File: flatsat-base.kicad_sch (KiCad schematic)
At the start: 13 parts, among them J1 xf2m-2415-1a-symbols, J10 Conn_01x24_Male, J11 Conn_02x05_Odd_Even, J12 Conn_02x05_Odd_Even, J13 Conn_01x10_Male, J2 XF2M-1015-1A-symbols, J3 XF2M-1015-1A-symbols, J4 XF2M-1015-1A-symbols, J5 XF2M-1015-1A-symbols, J6 XF2M-1015-1A-symbols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

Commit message: PCB outline and footprint locations defined, needs routing
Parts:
- J1: footprint PyCubed Main:XF2M-2415-1A -> PyCubed-Mini Main:XF2M-2415-1A
- J13: footprint Connector_PinHeader_1.27mm:PinHeader_1x10_P1.27mm_Vertical -> Connector_PinHeader_2.54mm:PinHeader_1x10_P2.54mm_Vertical
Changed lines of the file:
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@@
       (effects (font (size 1.27 1.27)) (justify right))
     )
-    (property "Footprint" "Connector_PinHeader_1.27mm:PinHeader_1x10_P1.27mm_Vertical" (id 2) (at 101.6 177.8 0)
+    (property "Footprint" "Connector_PinHeader_2.54mm:PinHeader_1x10_P2.54mm_Vertical" (id 2) (at 101.6 177.8 0)
       (effects (font (size 1.27 1.27)) hide)
     )
@@
     (property "Reference" "J1" (id 0) (at 54.61 30.48 0))
     (property "Value" "xf2m-2415-1a-symbols" (id 1) (at 54.61 33.02 0))
-    (property "Footprint" "PyCubed Main:XF2M-2415-1A" (id 2) (at 62.23 35.56 0)
+    (property "Footprint" "PyCubed-Mini Main:XF2M-2415-1A" (id 2) (at 62.23 35.56 0)
       (effects (font (size 1.27 1.27)) (justify left) hide)
     )
@@
     )
     (path "/eefa62b0-7985-4153-9454-98c24aeb544a"
-      (reference "J1") (unit 1) (value "xf2m-2415-1a-symbols") (footprint "PyCubed Main:XF2M-2415-1A")
+      (reference "J1") (unit 1) (value "xf2m-2415-1a-symbols") (footprint "PyCubed-Mini Main:XF2M-2415-1A")
     )
     (path "/405f63ce-92fd-4885-8744-aea1af979a53"
@@
     )
     (path "/cabb4d71-b835-4085-a569-a6974d8b4662"
-      (reference "J13") (unit 1) (value "Conn_01x10_Male") (footprint "Connector_PinHeader_1.27mm:PinHeader_1x10_P1.27mm_Vertical")
-    )
-  )
+      (reference "J13") (unit 1) (value "Conn_01x10_Male") (footprint "Connector_PinHeader_2.54mm:PinHeader_1x10_P2.54mm_Vertical")
+    )
+  )

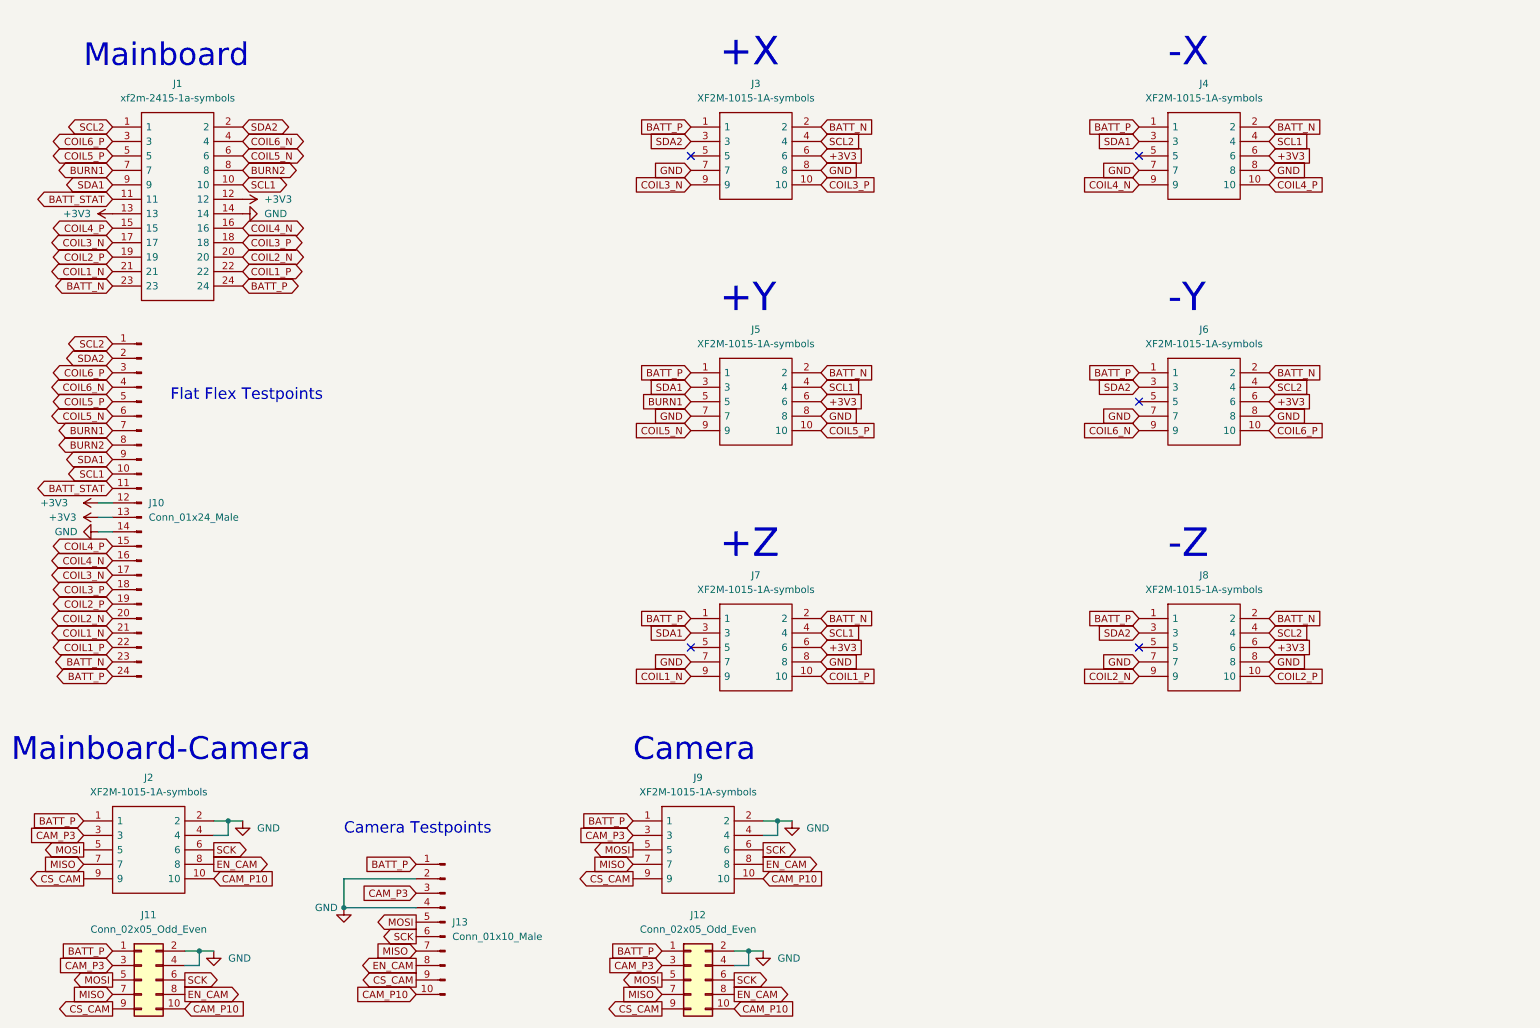
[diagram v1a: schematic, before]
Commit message: Shrank board size a little for cheaper production
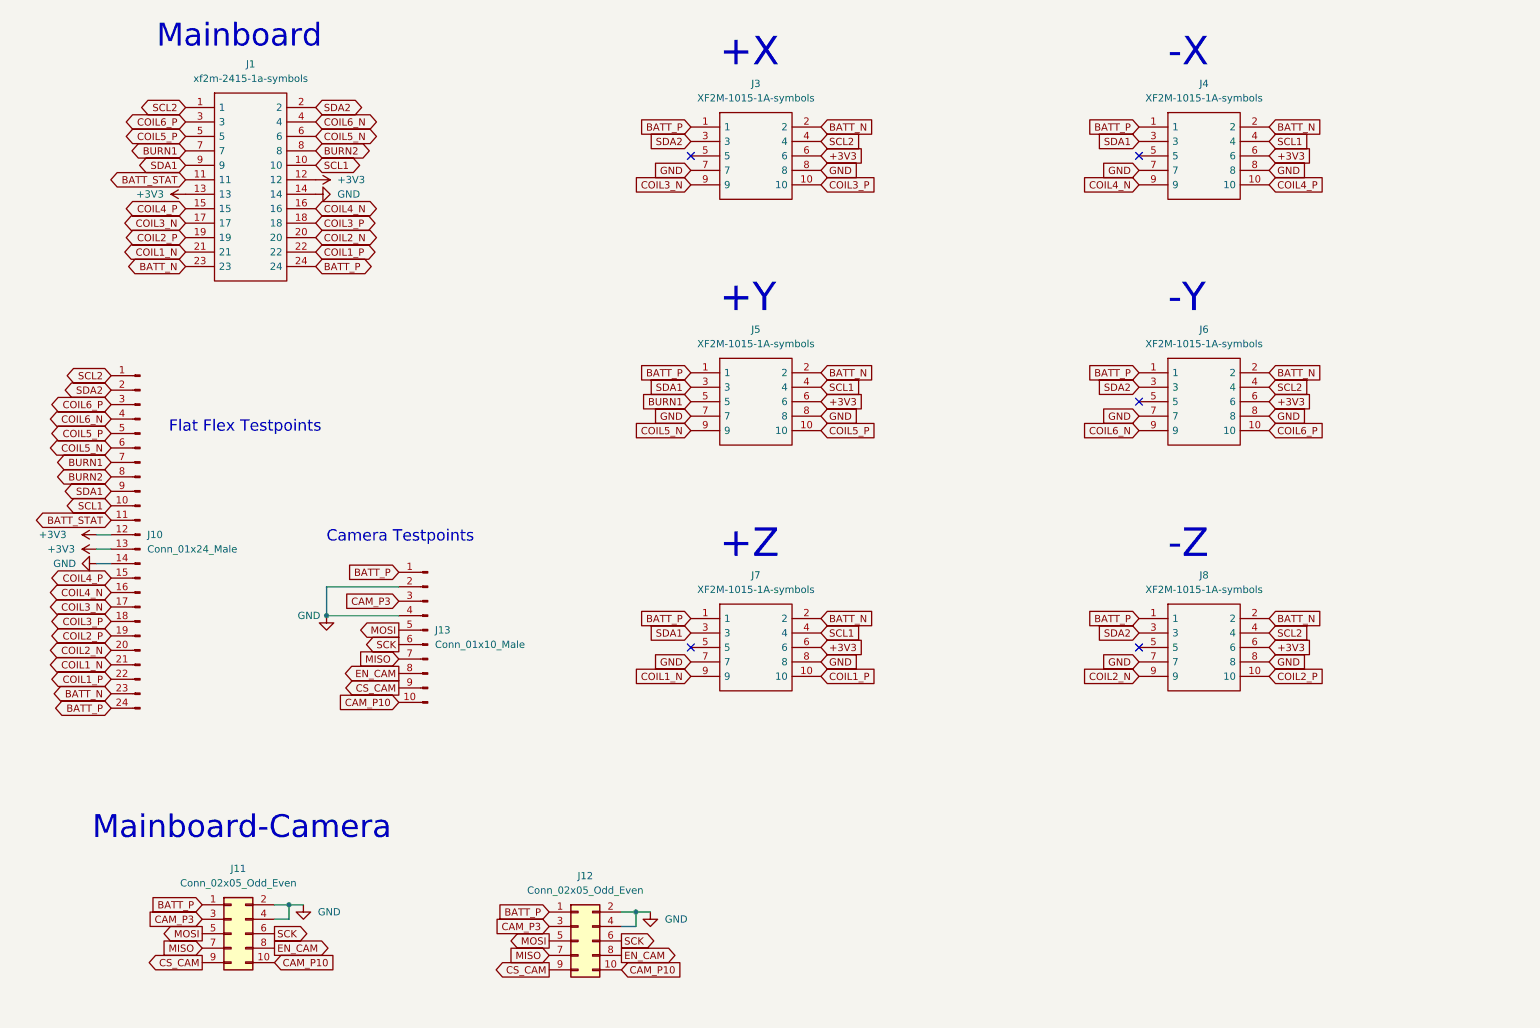
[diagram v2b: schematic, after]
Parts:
- removed J2, J9: XF2M-1015-1A-symbols, PyCubed-Mini Solar:XF2M-1015-1A, symbol PyCubed Mini avionics-motherboard:XF2M-1015-1A-symbols
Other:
- note removed: "Camera"
- moved on the sheet: J1, J10, J11, J12, J13

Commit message: Partially routed
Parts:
- J1: value xf2m-2415-1a-symbols -> (none); footprint PyCubed-Mini Main:XF2M-2415-1A -> (none); symbol PyCubed Mini avionics-motherboard:xf2m-2415-1a-symbols -> mainboard:FFC2B28-24-G
- J2: renamed from J3; value XF2M-1015-1A-symbols -> (none); footprint PyCubed-Mini Solar:XF2M-1015-1A -> solarpanels:GCT_FFC2B28-10-G; symbol PyCubed Mini avionics-motherboard:XF2M-1015-1A-symbols -> solarpanels:FFC2B28-10-G
- J3: renamed from J4; value XF2M-1015-1A-symbols -> (none); footprint PyCubed-Mini Solar:XF2M-1015-1A -> solarpanels:GCT_FFC2B28-10-G; symbol PyCubed Mini avionics-motherboard:XF2M-1015-1A-symbols -> solarpanels:FFC2B28-10-G
- J4: renamed from J5; value XF2M-1015-1A-symbols -> (none); footprint PyCubed-Mini Solar:XF2M-1015-1A -> solarpanels:GCT_FFC2B28-10-G; symbol PyCubed Mini avionics-motherboard:XF2M-1015-1A-symbols -> solarpanels:FFC2B28-10-G
- J5: renamed from J6; value XF2M-1015-1A-symbols -> (none); footprint PyCubed-Mini Solar:XF2M-1015-1A -> solarpanels:GCT_FFC2B28-10-G; symbol PyCubed Mini avionics-motherboard:XF2M-1015-1A-symbols -> solarpanels:FFC2B28-10-G
- J6: renamed from J7; value XF2M-1015-1A-symbols -> (none); footprint PyCubed-Mini Solar:XF2M-1015-1A -> solarpanels:GCT_FFC2B28-10-G; symbol PyCubed Mini avionics-motherboard:XF2M-1015-1A-symbols -> solarpanels:FFC2B28-10-G
- J7: renamed from J8; value XF2M-1015-1A-symbols -> (none); footprint PyCubed-Mini Solar:XF2M-1015-1A -> solarpanels:GCT_FFC2B28-10-G; symbol PyCubed Mini avionics-motherboard:XF2M-1015-1A-symbols -> solarpanels:FFC2B28-10-G
- J8: renamed from J11; footprint Connector_PinHeader_1.27mm:PinHeader_2x05_P1.27mm_Vertical -> (none)
- renumbered J13 to J11, J12 to J9
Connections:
- net CAM_P10: now also J11.6 (Pin_6); no longer J11.10 (Pin_10)
- net CAM_P3: now also J11.10 (Pin_10); no longer J11.3 (Pin_3)
- net CS_CAM: now also J11.7 (Pin_7); no longer J11.9 (Pin_9)
- net EN_CAM: now also J11.5 (Pin_5); no longer J11.8 (Pin_8)
- net GND: now also J11.3 (Pin_3); no longer J11.4 (Pin_4)
- net MISO: now also J11.8 (Pin_8); no longer J11.7 (Pin_7)
- net MOSI: now also J11.9 (Pin_9); no longer J11.5 (Pin_5)
- net SCK: now also J11.4 (Pin_4); no longer J11.6 (Pin_6)
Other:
- moved on the sheet: J1, J10, J11, J2, J3, J4, J5, J6, J7, J8, J9

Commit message: Finished routing
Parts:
- added H1, H2, H3, H4: MountingHole, symbol Mechanical:MountingHole
- J1: value (none) -> FFC2B28-24-G; footprint (none) -> mainboard:GCT_FFC2B28-24-G
- J2, J3, J4, J5, J6, J7: value (none) -> FFC2B28-10-G
- J8: footprint (none) -> Connector_PinSocket_1.27mm:PinSocket_2x05_P1.27mm_Vertical
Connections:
- net BATT_N: now also J1.2; no longer J1.23
- net BATT_P: now also J1.1; no longer J1.24
- net BATT_STAT: now also J1.14; no longer J1.11
- net BURN1: now also J1.18, J7.5; no longer J1.7, J4.5
- net BURN2: now also J1.17; no longer J1.8
- net COIL1_N: now also J1.4, J4.9; no longer J1.21, J6.9
- net COIL1_P: now also J1.3, J4.10; no longer J1.22, J6.10
- net COIL2_N: now also J1.5, J5.9; no longer J1.20, J7.9
- net COIL2_P: now also J1.6, J5.10; no longer J1.19, J7.10
- net COIL3_N: now also J1.8, J6.9; no longer J1.17, J2.9
- net COIL3_P: now also J1.7, J6.10; no longer J1.18, J2.10
- net COIL4_N: now also J1.9, J7.9; no longer J1.16, J3.9
- net COIL4_P: now also J1.10, J7.10; no longer J1.15, J3.10
- net COIL5_N: now also J1.19, J2.9; no longer J1.6, J4.9
- net COIL5_P: now also J1.20, J2.10; no longer J1.5, J4.10
- net COIL6_N: now also J1.21, J3.9; no longer J1.4, J5.9
- net COIL6_P: now also J1.22, J3.10; no longer J1.3, J5.10
- net GND: now also J1.11; no longer J1.14
- net SCL1: now also J1.15, J2.4; no longer J1.10, J3.4
- net SCL2: now also J1.24, J3.4; no longer J1.1, J2.4
- net SDA1: now also J1.16, J2.3; no longer J1.9, J3.3
- net SDA2: now also J1.23, J3.3; no longer J1.2, J2.3
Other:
- moved on the sheet: J10, J11

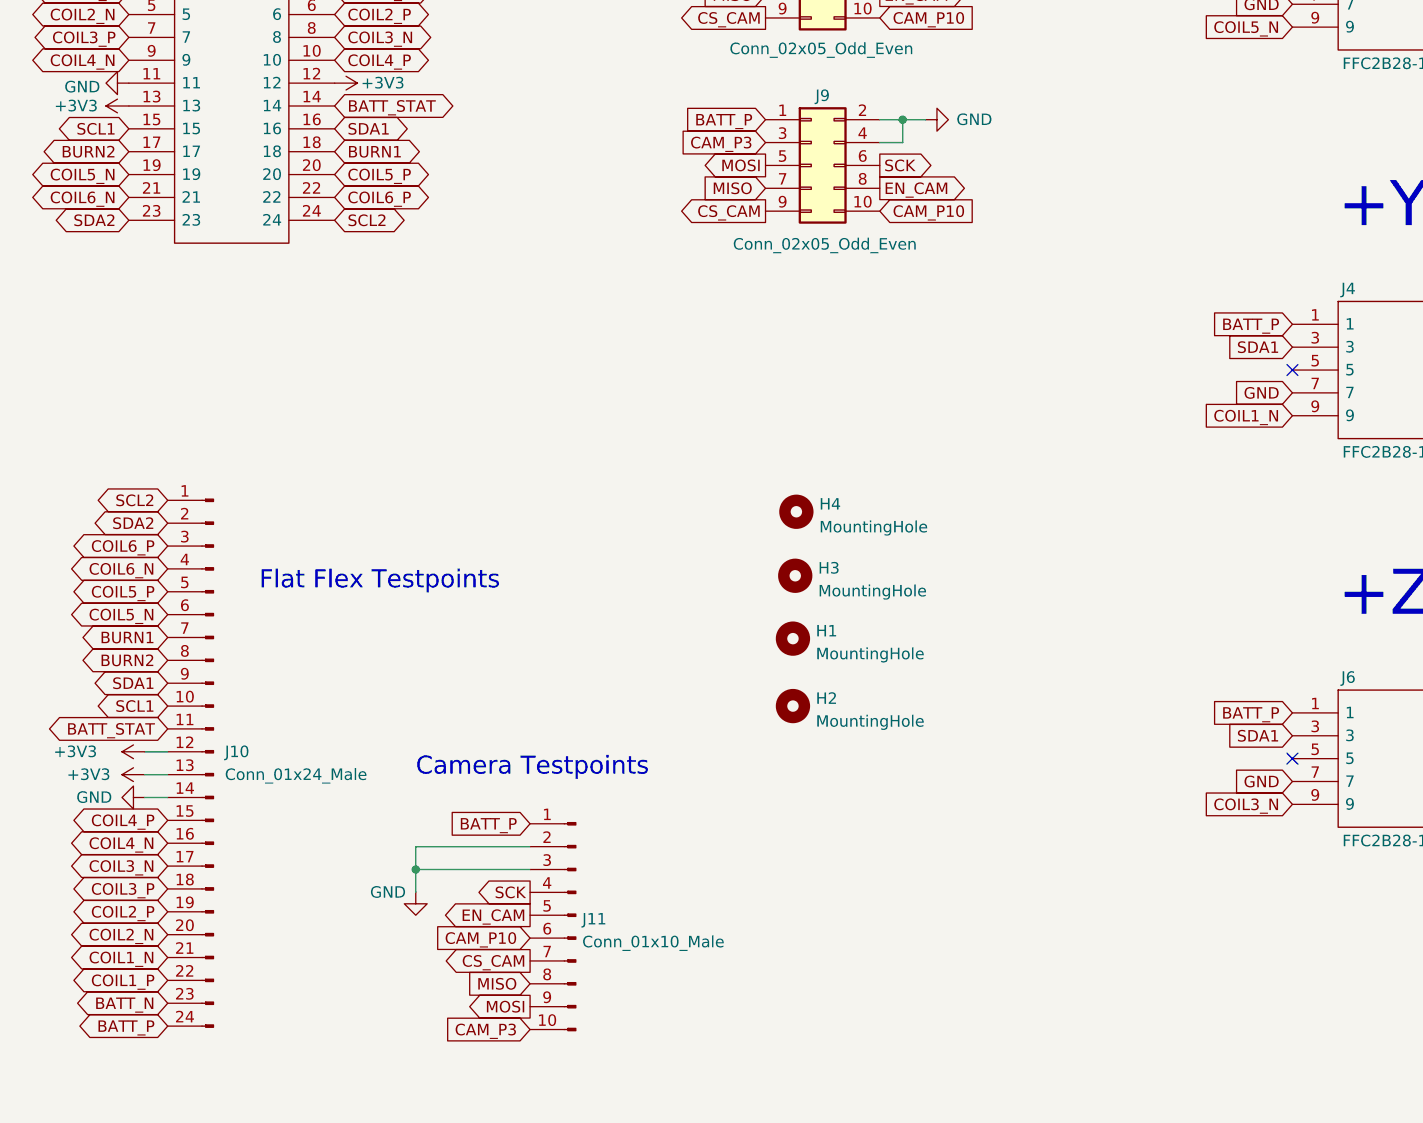
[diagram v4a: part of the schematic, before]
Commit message: Fixed Pinout on mainboard connector, added redundant flat-flex connector
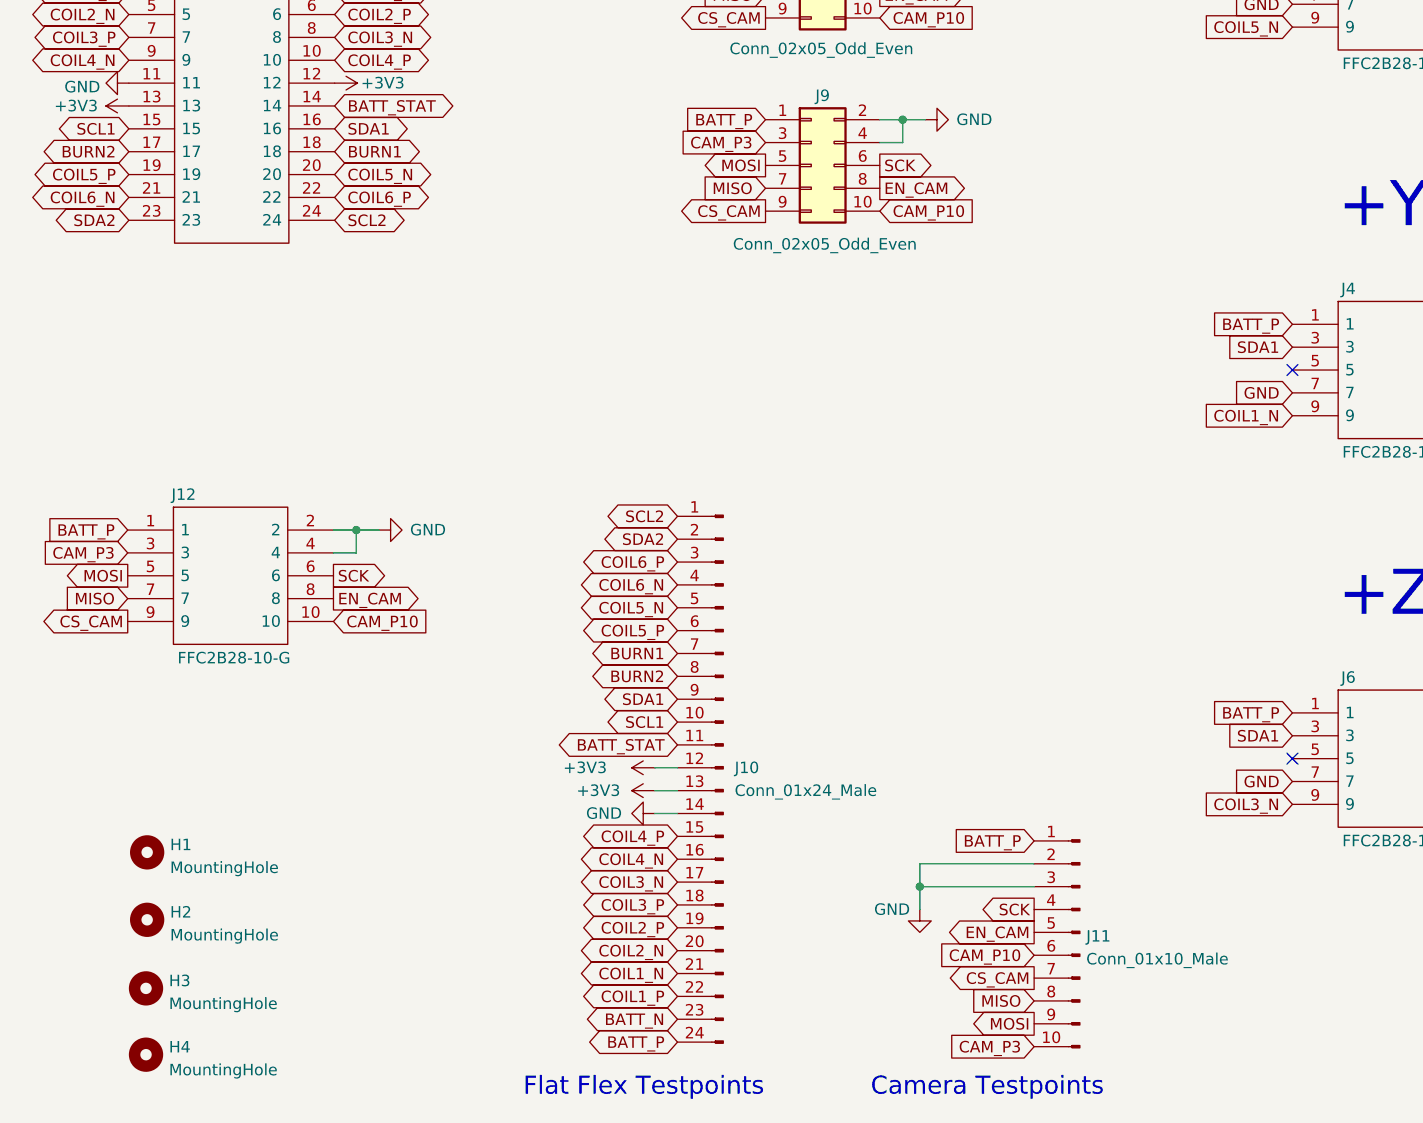
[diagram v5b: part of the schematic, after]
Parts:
- added J12: FFC2B28-10-G, solarpanels:GCT_FFC2B28-10-G, symbol solarpanels:FFC2B28-10-G
- H1, H2, H3, H4: footprint (none) -> MountingHole:MountingHole_3.2mm_M3_DIN965_Pad
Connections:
- net BATT_P: now also J12.1
- net CAM_P10: now also J12.10
- net CAM_P3: now also J12.3
- net COIL5_N: now also J1.20, J10.5 (Pin_5); no longer J1.19, J10.6 (Pin_6)
- net COIL5_P: now also J1.19, J10.6 (Pin_6); no longer J1.20, J10.5 (Pin_5)
- net CS_CAM: now also J12.9
- net EN_CAM: now also J12.8
- net GND: now also J12.2, J12.4
- net MISO: now also J12.7
- net MOSI: now also J12.5
- net SCK: now also J12.6
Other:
- moved on the sheet: H1, H2, H3, H4, J10, J11

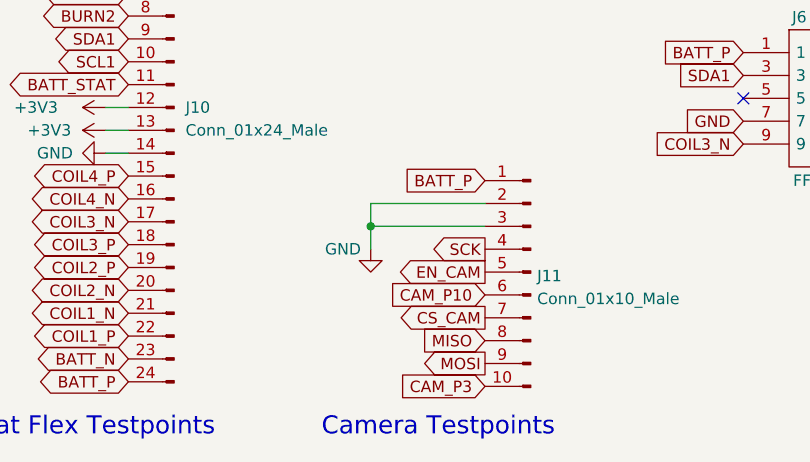
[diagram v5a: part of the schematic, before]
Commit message: Fixed some clearance issues, and re-routed Batt_P line
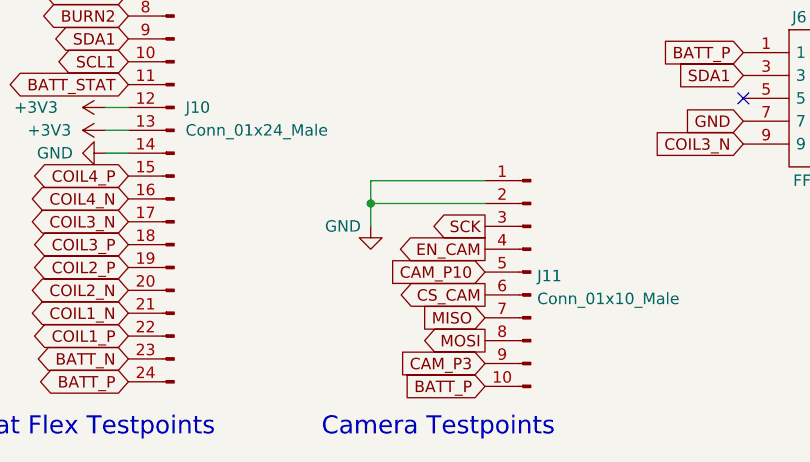
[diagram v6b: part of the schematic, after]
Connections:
- net BATT_P: now also J11.10 (Pin_10); no longer J11.1 (Pin_1)
- net CAM_P10: now also J11.5 (Pin_5); no longer J11.6 (Pin_6)
- net CAM_P3: now also J11.9 (Pin_9); no longer J11.10 (Pin_10)
- net CS_CAM: now also J11.6 (Pin_6); no longer J11.7 (Pin_7)
- net EN_CAM: now also J11.4 (Pin_4); no longer J11.5 (Pin_5)
- net GND: now also J11.1 (Pin_1); no longer J11.3 (Pin_3)
- net MISO: now also J11.7 (Pin_7); no longer J11.8 (Pin_8)
- net MOSI: now also J11.8 (Pin_8); no longer J11.9 (Pin_9)
- net SCK: now also J11.3 (Pin_3); no longer J11.4 (Pin_4)
